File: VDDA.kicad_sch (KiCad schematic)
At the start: 30 parts, among them J5 Conn_01x02, Q1 AO3401A, U6 L78M05ABDT-TR

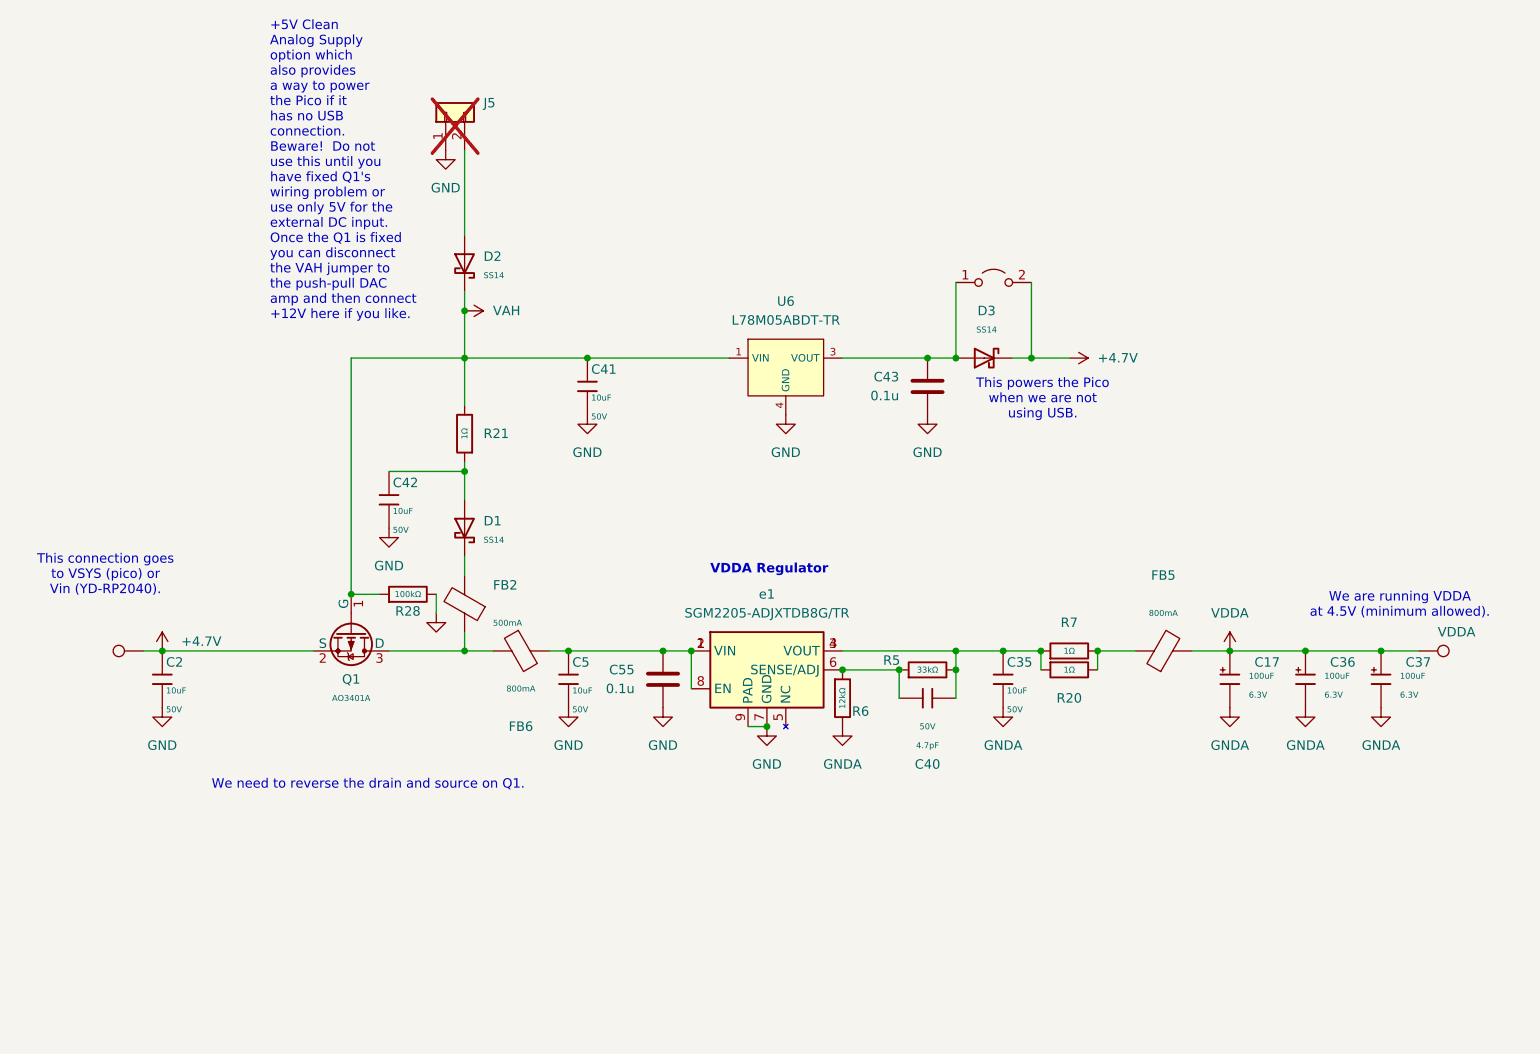
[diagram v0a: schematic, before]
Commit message: Starting a new branch for v0.2
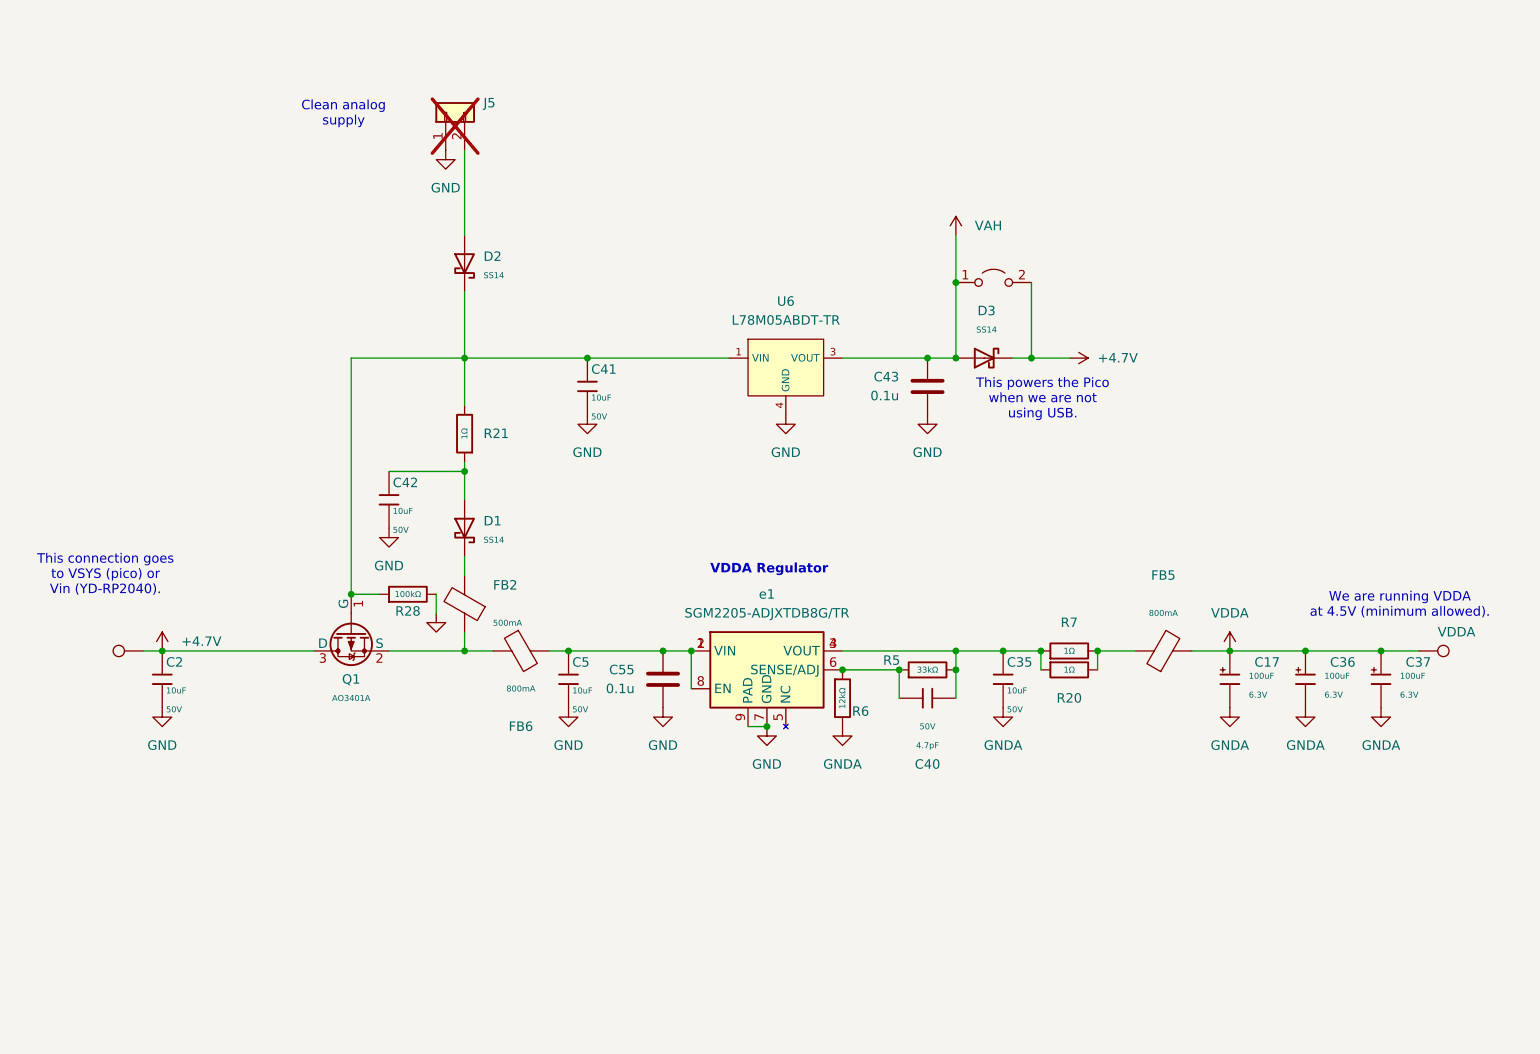
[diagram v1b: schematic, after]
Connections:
- net +4.7V: now also Q1.3 (D); no longer Q1.2 (S)
- net VAH: now also C43.1, D3.2, JP2.1 (A), U6.3 (VOUT); no longer C41.1, D2.1, Q1.1 (G), R21.2, R28.1, U6.1 (VIN)
- net at FB2.1, FB6.1: now also Q1.2 (S); no longer Q1.3 (D)
- new net: C41.1, D2.1, Q1.1 (G), R21.2, R28.1, U6.1 (VIN)
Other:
- note added: "Clean analog supply"
- note removed: "+5V Clean Analog Supply option which also provides a way to power the Pico if it has no USB connection. Beware! Do not use this until you have fixed Q1's wiring problem or use only 5V for the external DC input. Once the Q1 is fixed you can disconnect the VAH jumper to the push-pull DAC amp and then connect +12V here if you like."
- note removed: "We need to reverse the drain and source on Q1."
- moved on the sheet: Q1
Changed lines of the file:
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@@
 	(title_block
 		(date "2026-04-14")
-		(rev "v 0.1 errrors noted")
+		(rev "v 0.2")
 	)
 	(text "VDDA Regulator"
@@
 		)
 	)
-	(text "We need to reverse the drain and source on Q1."
-		(exclude_from_sim no)
-		(at 89.916 131.064 0)
-		(effects
-			(font
-				(size 1.27 1.27)
-				(color 255 4 41 1)
-			)
-		)
-	)
 	(text "We are running VDDA\nat 4.5V (minimum allowed)."
 		(exclude_from_sim no)
@@
 		)
 	)
-	(text "This powers the Pico\nwhen we are not \nusing USB."
+	(text "Clean analog\nsupply"
 		(exclude_from_sim no)
-		(at 180.594 79.248 0)
+		(at 86.614 40.894 0)
 		(effects
 			(font
@@
 		)
 	)
-	(text "+5V Clean \nAnalog Supply\noption which\nalso provides\na way to power\nthe Pico if it\nhas no USB \nconnection.\nBeware!  Do not\nuse this until you\nhave fixed Q1's \nwiring problem or \nuse only 5V for the\nexternal DC input.\nOnce the Q1 is fixed\nyou can disconnect\nthe VAH jumper to\nthe push-pull DAC\namp and then connect\n+12V here if you like."
+	(text "This powers the Pico\nwhen we are not \nusing USB."
 		(exclude_from_sim no)
-		(at 76.708 48.514 0)
+		(at 180.594 79.248 0)
 		(effects
 			(font
 				(size 1.27 1.27)
-				(color 255 2 79 1)
 			)
-			(justify left)
 		)
 	)
@@
 	)
 	(junction
+		(at 168.91 63.5)
+		(diameter 0)
+		(color 0 0 0 0)
+	)
+	(junction
 		(at 175.26 113.03)
 		(diameter 0)
@@
 	)
 	(junction
-		(at 102.87 67.31)
-		(diameter 0)
-		(color 0 0 0 0)
-	)
-	(junction
 		(at 161.29 115.57)
 		(diameter 0)
@@
 	(wire
 		(pts
-			(xy 102.87 64.77) (xy 102.87 67.31)
+			(xy 102.87 64.77) (xy 102.87 73.66)
 		)
 		(stroke
@@
 	(wire
 		(pts
+			(xy 168.91 57.15) (xy 168.91 63.5)
+		)
+		(stroke
+			(width 0)
+			(type default)
+		)
+	)
+	(wire
+		(pts
 			(xy 102.87 87.63) (xy 102.87 88.9)
 		)
@@
 	(wire
 		(pts
-			(xy 102.87 67.31) (xy 102.87 73.66)
-		)
-		(stroke
-			(width 0)
-			(type default)
-		)
-	)
-	(wire
-		(pts
 			(xy 59.69 113.03) (xy 62.23 113.03)
 		)
@@
 	(symbol
 		(lib_id "PCM_JLCPCB-Transistors:PMOS,AO3401A")
-		(at 87.63 110.49 270)
+		(at 87.63 110.49 90)
+		(mirror x)
 		(unit 1)
 		(body_style 1)
@@
 	(symbol
 		(lib_id "power:VDDA")
-		(at 102.87 67.31 270)
+		(at 168.91 57.15 0)
 		(unit 1)
 		(body_style 1)
@@
 		(fields_autoplaced yes)
 		(property "Reference" "#PWR093"
-			(at 99.06 67.31 0)
+			(at 168.91 60.96 0)
 			(hide yes)
 			(show_name no)
@@
 		)
 		(property "Value" "VAH"
-			(at 106.68 67.3099 90)
+			(at 171.45 55.8799 0)
 			(show_name no)
 			(do_not_autoplace no)
@@
 		)
 		(property "Footprint" ""
-			(at 102.87 67.31 0)
+			(at 168.91 57.15 0)
 			(hide yes)
 			(show_name no)
@@
 		)
 		(property "Datasheet" ""
-			(at 102.87 67.31 0)
+			(at 168.91 57.15 0)
 			(hide yes)
 			(show_name no)
@@
 		)
 		(property "Description" ""
-			(at 102.87 67.31 0)
+			(at 168.91 57.15 0)
 			(hide yes)
 			(show_name no)

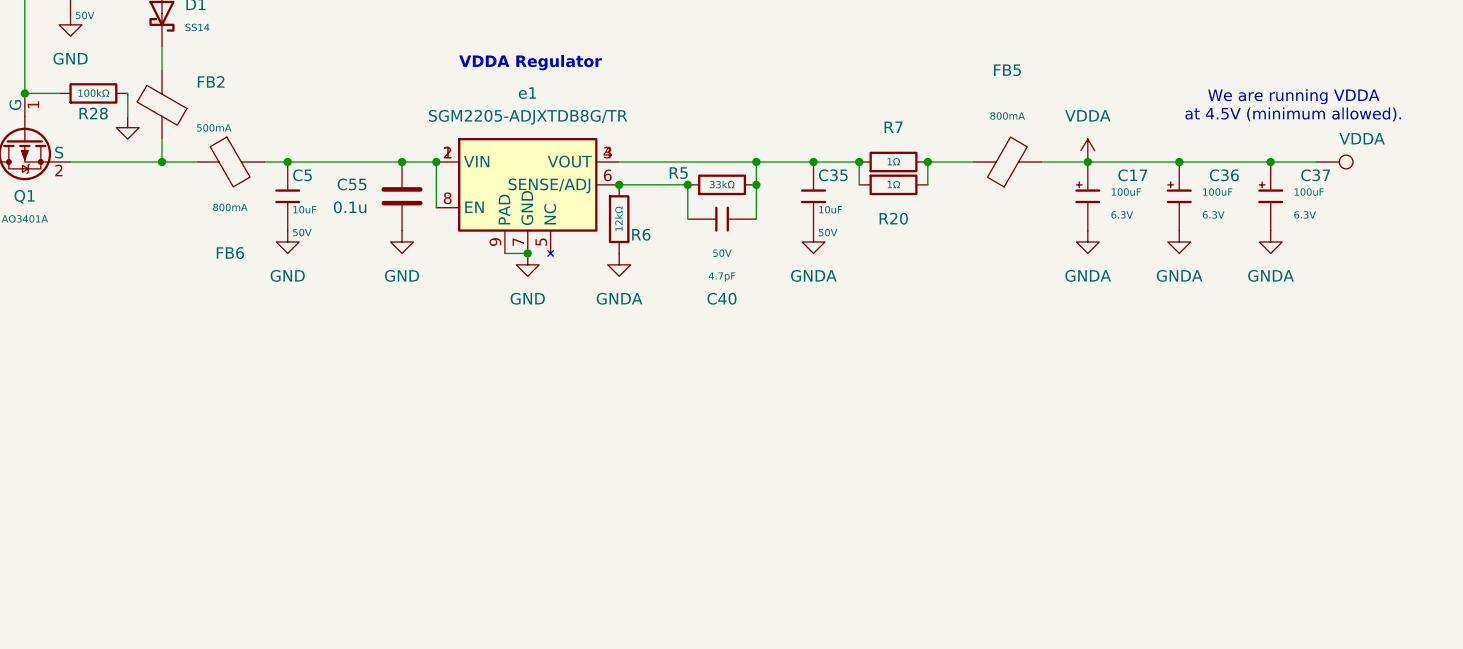
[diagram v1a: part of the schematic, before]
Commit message: Adding fixes:
LDO for LO.  Reduce gain by 10/1.5.  Add better bypassing for VDDA/2 and CMOS Oscillator.  Added Johnson counter.  This is schematic only at the moment.
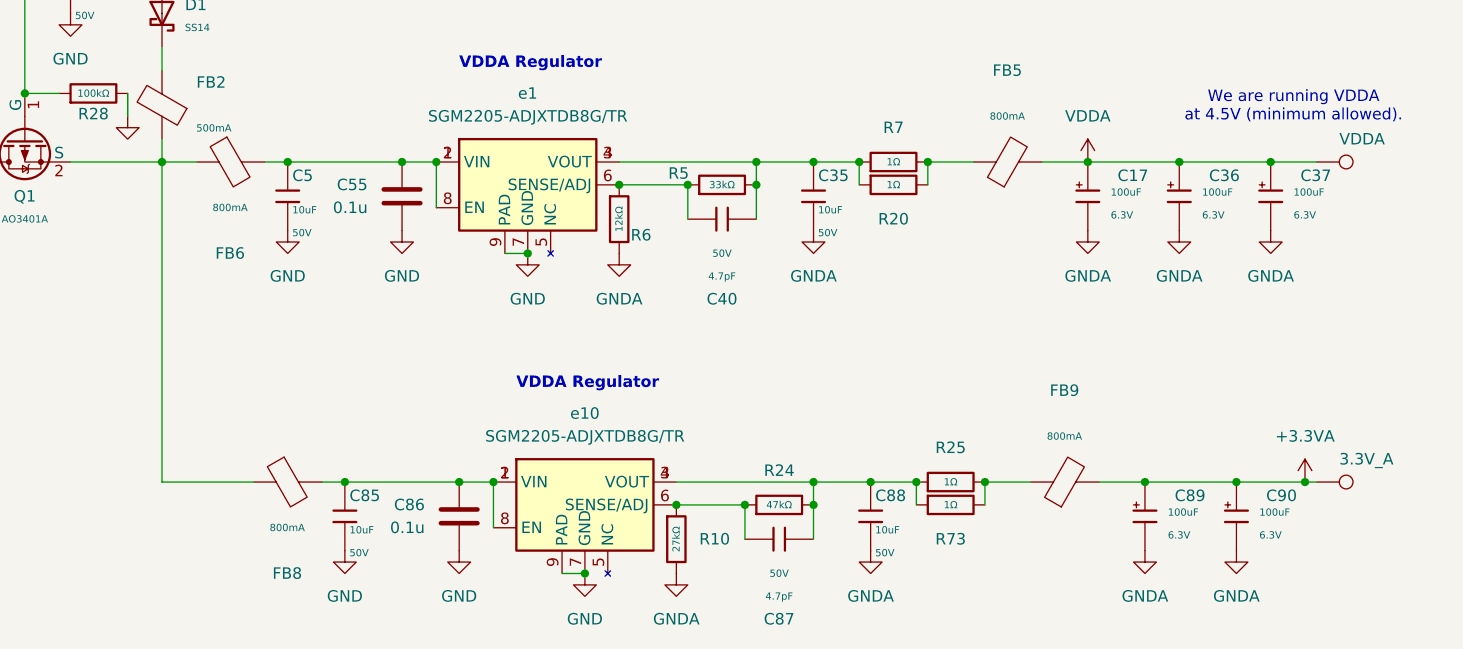
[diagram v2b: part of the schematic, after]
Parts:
- added C85, C88: 10uF, PCM_JLCPCB:C_1206, symbol PCM_JLCPCB-Capacitors:1206,10uF
- added C86: 0.1u, Capacitor_SMD:C_0805_2012Metric, symbol Device:C
- added C87: 4.7pF, PCM_JLCPCB:C_0603, symbol PCM_JLCPCB-Capacitors:0603,4.7pF
- added C89, C90: 100uF, PCM_JLCPCB:C_CASE-B-3528-21(mm), symbol PCM_JLCPCB-Capacitors:CASE-B-3528-21(mm),100uF
- added FB8, FB9: (no value), PCM_JLCPCB:FB_0805, symbol PCM_JLCPCB-Inductors:Ferrite,0805
- added R10: 27kΩ, PCM_JLCPCB:R_0805, symbol PCM_JLCPCB-Resistors:0805,27kΩ
- added R24: 47kΩ, PCM_JLCPCB:R_0805, symbol PCM_JLCPCB-Resistors:0805,47kΩ
- added R25, R73: 1Ω, PCM_JLCPCB:R_0805, symbol PCM_JLCPCB-Resistors:0805,1Ω
- added TP27: 3.3V_A, TestPoint:TestPoint_THTPad_D1.5mm_Drill0.7mm, symbol Connector:TestPoint
- added e10: SGM2205-ADJXTDB8G/TR, Package_DFN_QFN:DFN-8-1EP_3x3mm_P0.65mm_EP1.55x2.4mm, symbol Regulator_Linear:ADP7142AUJZ
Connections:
- net GND: now also C85.2, C86.2, e10.7 (GND), e10.9 (PAD)
- net GNDA: now also C88.2, C89.2, C90.2, R10.2
- net at FB2.1, FB6.1, Q1.2 (S): now also FB8.1
- new net: C85.1, C86.1, FB8.2, e10.1 (VIN), e10.2 (VIN), e10.8 (EN)
- new net: C87.1, C88.1, R24.2, R25.1, R73.1, e10.3 (VOUT), e10.4 (VOUT)
- new net: FB9.1, R25.2, R73.2
- new net: C87.2, R10.1, R24.1, e10.6 (SENSE/ADJ)
- new net +3.3VA: C89.1, C90.1, FB9.2, TP27.1

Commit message: Saved schematic
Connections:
- net VAH: no longer names the net of C43.1, D3.2, JP2.1 (A), U6.3 (VOUT)
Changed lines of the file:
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@@
 	)
 	(junction
-		(at 168.91 63.5)
-		(diameter 0)
-		(color 0 0 0 0)
-	)
-	(junction
 		(at 175.26 113.03)
 		(diameter 0)
@@
 	)
 	(junction
+		(at 179.07 63.5)
+		(diameter 0)
+		(color 0 0 0 0)
+	)
+	(junction
 		(at 129.54 113.03)
 		(diameter 0)
@@
 	(wire
 		(pts
-			(xy 168.91 57.15) (xy 168.91 63.5)
+			(xy 179.07 57.15) (xy 179.07 63.5)
 		)
 		(stroke
@@
 	(symbol
 		(lib_id "power:VDDA")
-		(at 168.91 57.15 0)
+		(at 179.07 57.15 0)
 		(unit 1)
 		(body_style 1)
@@
 		(fields_autoplaced yes)
 		(property "Reference" "#PWR093"
-			(at 168.91 60.96 0)
+			(at 179.07 60.96 0)
 			(hide yes)
 			(show_name no)
@@
 		)
 		(property "Value" "VAH"
-			(at 171.45 55.8799 0)
+			(at 181.61 55.8799 0)
 			(show_name no)
 			(do_not_autoplace no)
@@
 		)
 		(property "Footprint" ""
-			(at 168.91 57.15 0)
+			(at 179.07 57.15 0)
 			(hide yes)
 			(show_name no)
@@
 		)
 		(property "Datasheet" ""
-			(at 168.91 57.15 0)
+			(at 179.07 57.15 0)
 			(hide yes)
 			(show_name no)
@@
 		)
 		(property "Description" ""
-			(at 168.91 57.15 0)
+			(at 179.07 57.15 0)
 			(hide yes)
 			(show_name no)

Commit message: Placed the second ADC
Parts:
- C17, C36, C37, C89, C90: Manufacturer AVX -> (none)
- C2, C35, C41, C42, C5, C85, C88: Manufacturer Samsung Electro-Mechanics -> (none)
- C40, C87: Manufacturer FH(Guangdong Fenghua Advanced Tech) -> (none)
- D1, D2, D3: Manufacturer MDD（Microdiode Electronics） -> (none)
- FB2, FB5, FB6, FB8, FB9: Manufacturer Sunlord -> (none)
- Q1: Manufacturer Alpha & Omega Semicon -> (none)
- R10, R20, R21, R24, R25, R28, R5, R6, R7, R73: Manufacturer UNI-ROYAL(Uniroyal Elec) -> (none)
- TP26, TP27: footprint TestPoint:TestPoint_THTPad_D1.5mm_Drill0.7mm -> TestPoint:TestPoint_THTPad_D2.0mm_Drill1.0mm
- U6: Manufacturer STMicroelectronics -> (none)

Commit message: More routing
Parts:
- TP25: footprint TestPoint:TestPoint_THTPad_D1.5mm_Drill0.7mm -> TP_Label:TestPoint_THTPad_D2.0mm_Drill1.0mm
- TP26, TP27: footprint TestPoint:TestPoint_THTPad_D2.0mm_Drill1.0mm -> TP_Label:TestPoint_THTPad_D2.0mm_Drill1.0mm
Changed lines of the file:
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@@
 			)
 		)
-		(property "Footprint" "TestPoint:TestPoint_THTPad_D1.5mm_Drill0.7mm"
+		(property "Footprint" "TP_Label:TestPoint_THTPad_D2.0mm_Drill1.0mm"
 			(at 59.69 107.95 0)
 			(hide yes)
@@
 			)
 		)
-		(property "Footprint" "TestPoint:TestPoint_THTPad_D2.0mm_Drill1.0mm"
+		(property "Footprint" "TP_Label:TestPoint_THTPad_D2.0mm_Drill1.0mm"
 			(at 231.14 153.67 0)
 			(hide yes)
@@
 			)
 		)
-		(property "Footprint" "TestPoint:TestPoint_THTPad_D2.0mm_Drill1.0mm"
+		(property "Footprint" "TP_Label:TestPoint_THTPad_D2.0mm_Drill1.0mm"
 			(at 231.14 118.11 0)
 			(hide yes)

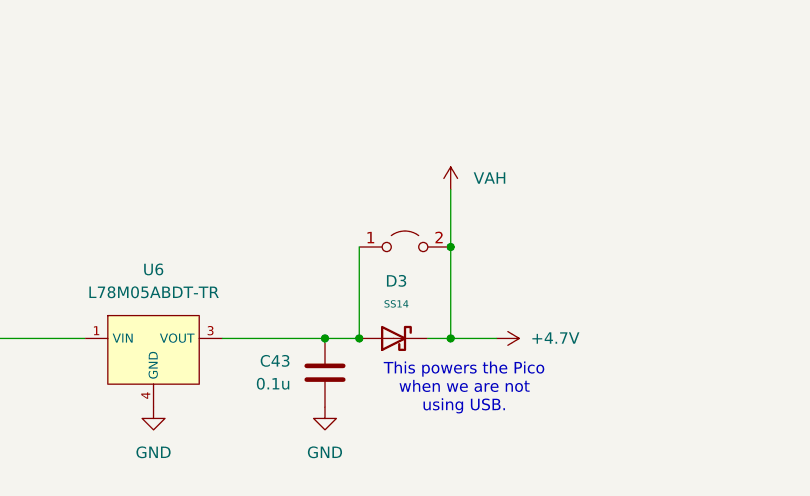
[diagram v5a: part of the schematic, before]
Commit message: Fixed sub-schematic versions
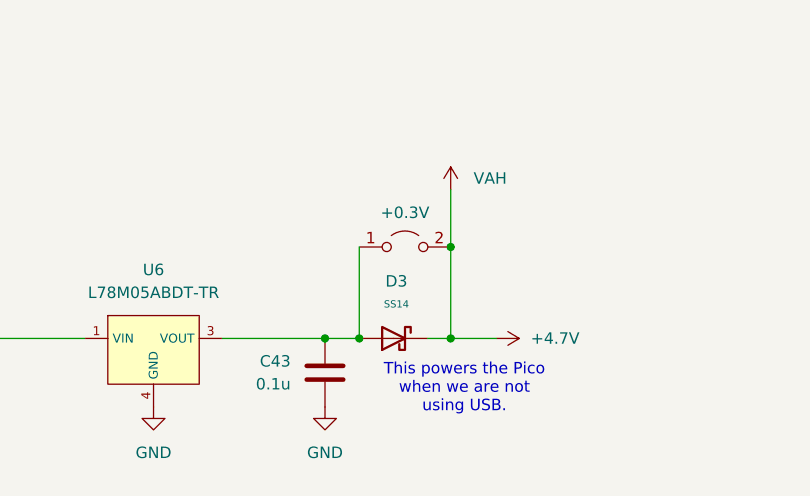
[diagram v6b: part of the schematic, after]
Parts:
- JP2: value (none) -> +0.3V
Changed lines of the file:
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@@
 			)
 		)
-		(property "Value" ""
+		(property "Value" "+0.3V"
 			(at 173.99 59.69 0)
 			(show_name no)

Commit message: Label Tweaks
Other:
- note added: "Clean analog supply (+5 to +15 V)"
- note removed: "Clean analog supply"
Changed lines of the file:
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@@
 		)
 	)
-	(text "Clean analog\nsupply"
+	(text "Clean analog\nsupply \n(+5 to +15 V)"
 		(exclude_from_sim no)
 		(at 86.614 40.894 0)
